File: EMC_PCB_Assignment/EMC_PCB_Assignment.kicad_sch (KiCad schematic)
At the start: 58 parts, among them IC1 LT8636JV#PBF, IC2 LP2985AIM5-3.0_NOPB, IC3 ATMEGA16U2-MU, IC4 ATMEGA328P-PU, IC5 OPA4350UA, J1 61300621121, J2 61300621121, J3 Header 8, J4 61300821121, J5 Header 10, J6 61300421121, J7 USB_B_Micro, Y1 16M, Y2 16M

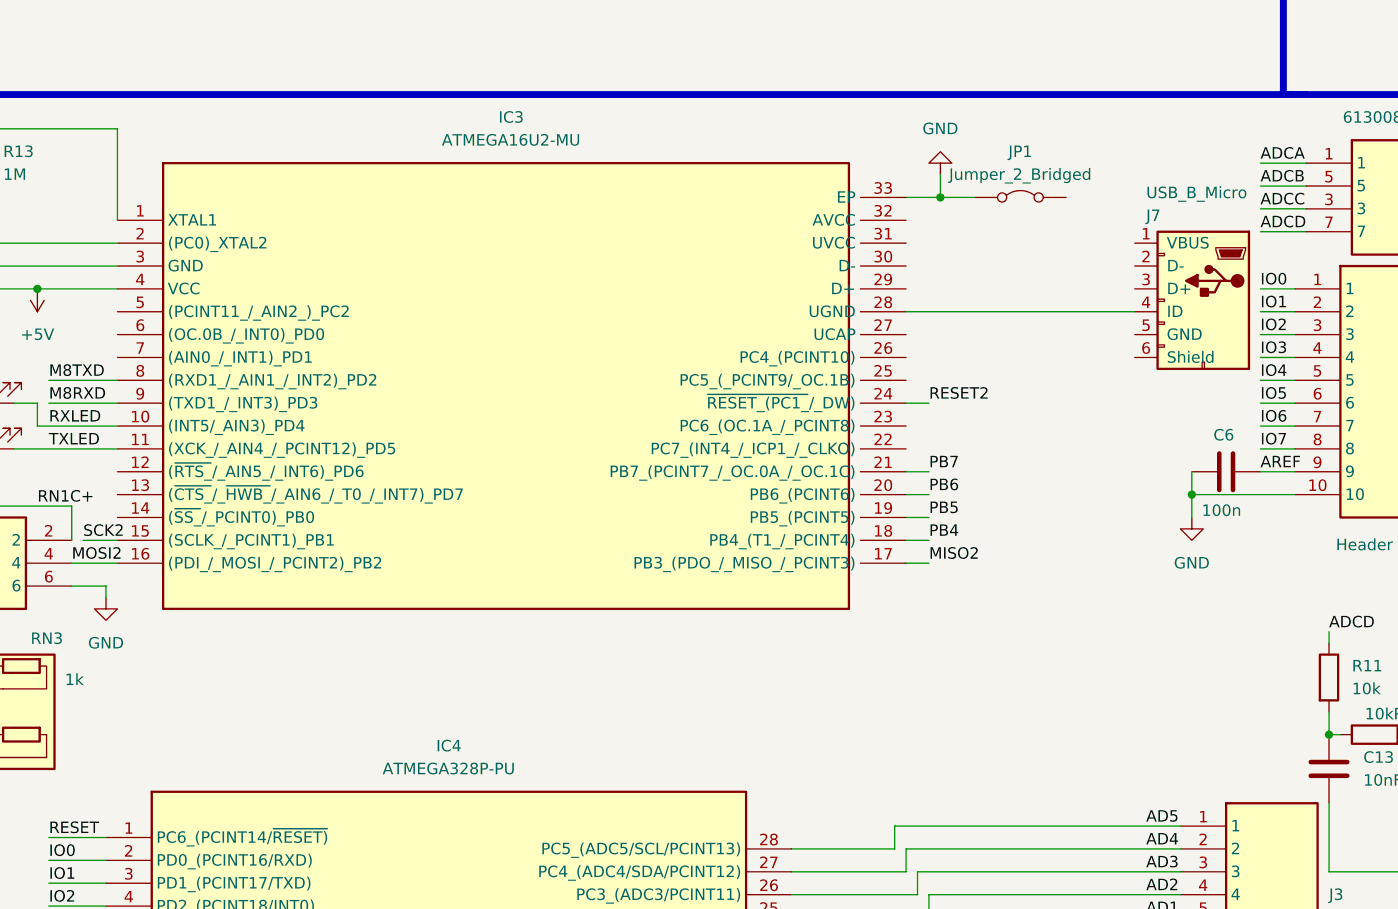
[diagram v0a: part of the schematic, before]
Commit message: Only LT8636 is still missing
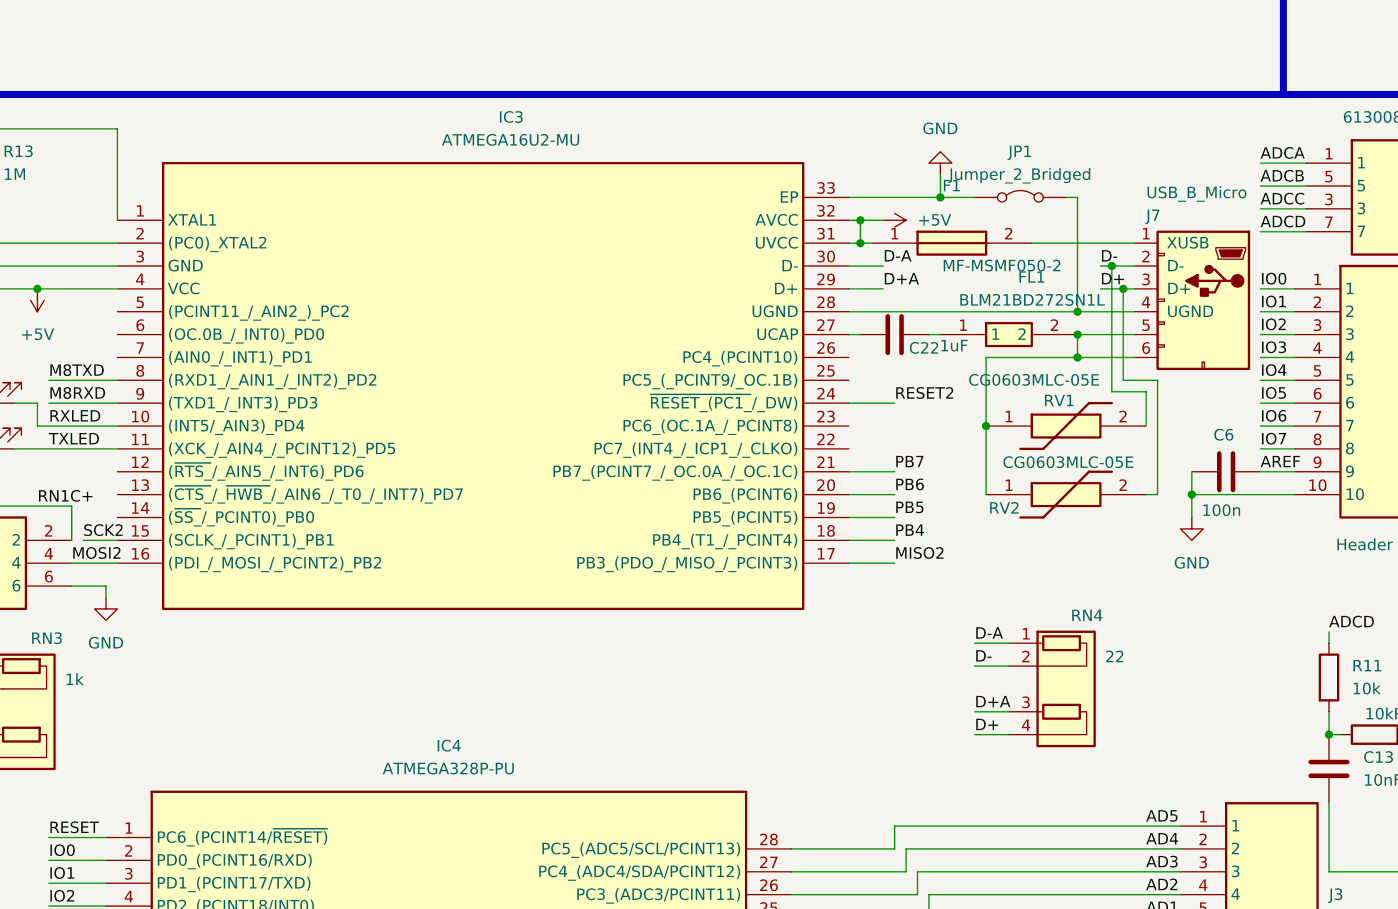
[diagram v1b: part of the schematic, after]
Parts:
- added C22: 1uF, symbol Device:C
- added F1: MF-MSMF050-2, FUSC4632X85N, symbol SamacSys_Parts:MF-MSMF050-2
- added FL1: BLM21BD272SN1L, BLM21BD222SH1K, symbol SamacSys_Parts:BLM21BD272SN1L
- added RN4: 22, Resistor_THT:R_Array_SIP4, symbol Device:R_Pack02_SIP
- added RV1, RV2: CG0603MLC-05E, VARC1608X55N, symbol SamacSys_Parts:CG0603MLC-05E
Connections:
- net +5V: now also IC3.31 (UVCC), IC3.32 (AVCC), F1.1
- net at IC3.27 (UCAP): now also C22.1
- net at IC3.28 (UGND), J7.4 (UGND): now also JP1.2 (B)
- net D+A: now reaches IC3.29 (D+)
- net D+A: now also RN4.3 (R2.1)
- net D-A: now reaches IC3.30 (D-)
- net D-A: now also RN4.1 (R1.1)
- net at J7.1 (XUSB): now also F1.2
- net D-: now reaches J7.2 (D-)
- net D-: now also RN4.2 (R1.2), RV1.2
- net D+: now reaches J7.3 (D+)
- net D+: now also RN4.4 (R2.2), RV2.2
- net at J7.5: now also J7.6, FL1.2, RV1.1, RV2.1
- new net: C22.2, FL1.1
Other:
- moved on the sheet: IC3

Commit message: Schematics Finished. I also put the imported Components in there. I was not sure if they are also in the project itself
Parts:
- removed RN1: 1k, Resistor_THT:R_Array_SIP4, symbol Device:R_Pack02_SIP
- added C, C29, C30: 1uF, symbol Device:C
- added C23, C24, C25: 10uF, symbol Device:C
- added C26: 100uF, symbol Device:C
- added C27: 0.1uF, symbol Device:C
- added C28: 10pF, symbol Device:C
- added D5: LED, symbol Device:LED
- added FB1: FerriteBead, symbol Device:FerriteBead
- added J8: Power Connector, SHDRRA2W80P0X350_1X2_1050X920X750P, symbol SamacSys_Parts:691305140002
- added L2: 0.33u, symbol Device:L
- added L3: 1.5u, symbol Device:L
- added R15: 1M, symbol Device:R
- added R16: 243k, symbol Device:R
- added R17: 17.8k, symbol Device:R
- added RN5: 1k, symbol Device:R_Pack04
- J1, J2: value 61300621121 -> 3x2 Connector
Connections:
- net +5V: now also IC1.2 (BIAS), C26.2, C28.2, L3.1, R15.2, RN5.7 (R2.2), RN5.8 (R1.2)
- net GND: now also IC1.4 (GND_1), C.1, C23.2, C24.2, C25.2, C26.1, D5.1 (K), J8.2
- net IO0: now also RN5.4 (R4.1)
- net IO1: now also RN5.3 (R3.1)
- net M8RXD: now also RN5.5 (R4.2)
- net M8TXD: now also RN5.6 (R3.2)
- net at IC1.10 (SW_3): now also IC1.8 (SW_1), IC1.9 (SW_2), C27.1, L3.2
- net VIN: now reaches IC1.11 (VIN_2)
- net VIN: now also IC1.14 (EN/UV), C30.1
- net at IC1.13 (GND_2): now also IC1.21 (GND_3), C29.2, C30.2, R16.2, R17.2
- net INTVCC: now reaches IC1.15 (SYNC/MODE)
- net INTVCC: now also IC1.3 (INTVCC), C29.1
- net at IC1.17 (RT): now also R17.1
- net FB: now reaches IC1.19 (FB_1)
- net FB: now also IC1.20 (FB_2), C28.1, R15.1, R16.1
- net at IC1.6 (VIN_1): now also C.2, C25.1, L2.2
- net at IC1.7 (BST): now also C27.2
- new net: C24.1, FB1.2, L2.1
- new net P_LED_IN: D5.2 (A), RN5.1 (R1.1), RN5.2 (R2.1)
- new net VCC: C23.1, FB1.1, J8.1
- no-connect marks 0 -> 17
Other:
- note added: "See RN5 on the Schematics"
- note added: "Vout (5V)"
- company: (none) -> Group 16
- title: (none) -> Microcontroller_PCB_Assignment
- moved on the sheet: IC1, RV1, RV2

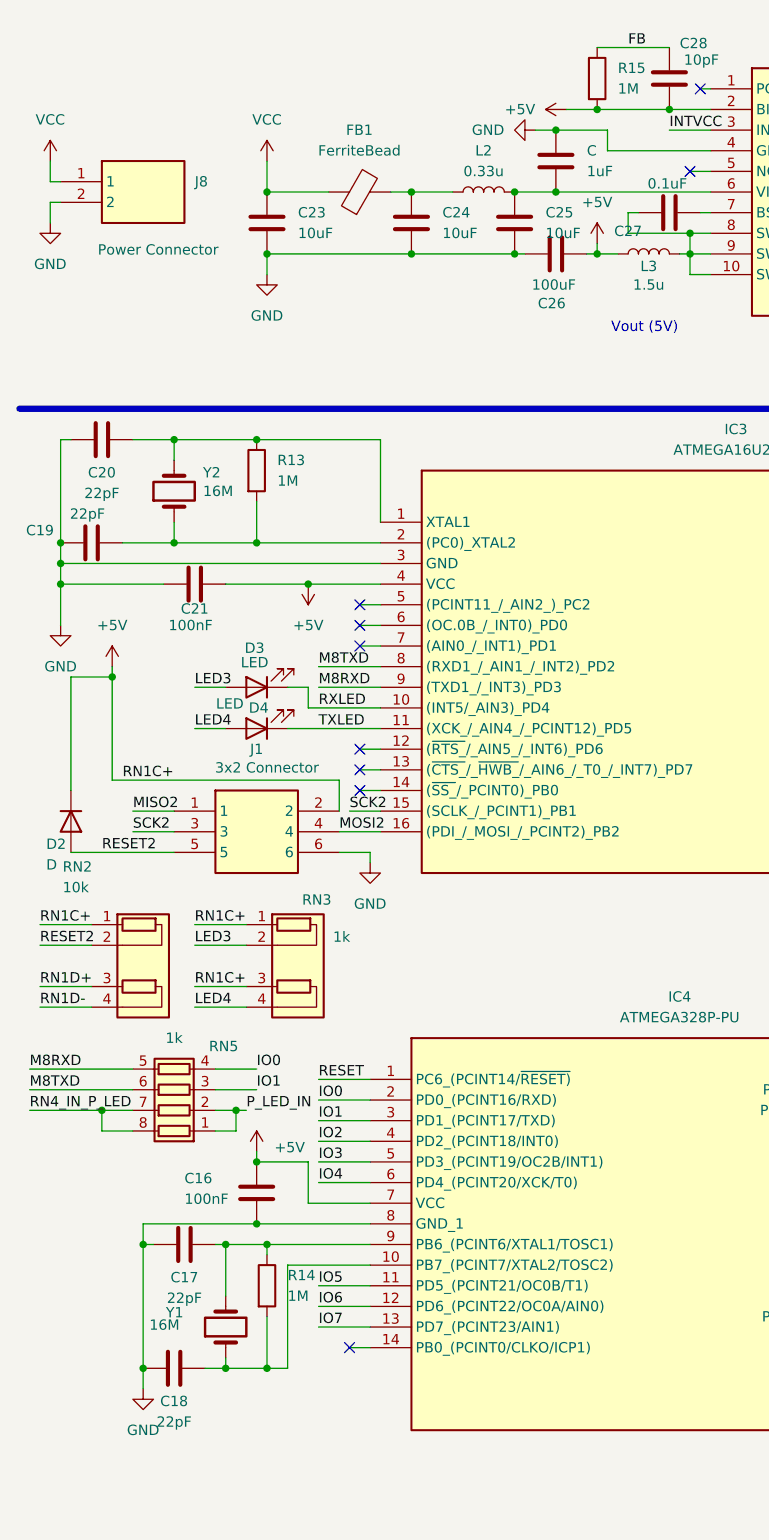
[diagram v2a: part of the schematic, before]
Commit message: Added Footprint libraries and footprints to all components
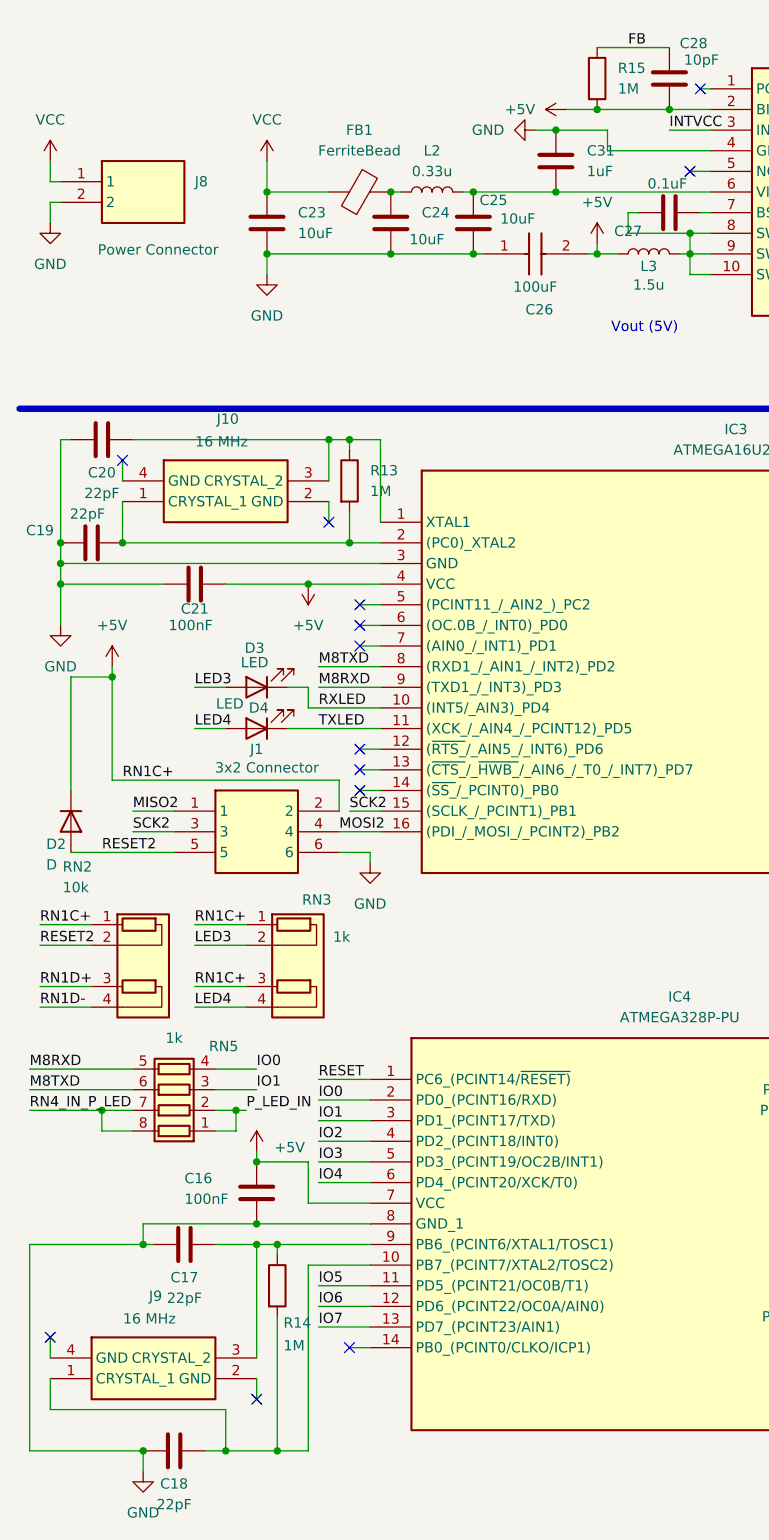
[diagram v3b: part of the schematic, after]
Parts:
- removed C26: 100uF, symbol Device:C
- removed Y1, Y2: 16M, symbol Device:Crystal
- added C26: 100uF, SamacSys_Parts:CAPPM3528X210N, symbol SamacSys_Parts:NOJB107M006RWJ
- added J10, J9: 16 MHz, SamacSys_Parts:LFXTAL062487Cutt, symbol SamacSys_Parts:LFXTAL062487Cutt
- C1, C10, C11, C12, C13, C14, C15, C16, C17, C18, C19, C2, C20, C21, C22, C23, C24, C25, C27, C28, C29, C3, C30, C4, C5, C6, C7, C8, C9: footprint (none) -> Capacitor_SMD:C_0402_1005Metric
- C31: renamed from C; footprint (none) -> Capacitor_SMD:C_0402_1005Metric
- D1, D2: footprint (none) -> Diode_SMD:D_0402_1005Metric
- D3, D4, D5: footprint (none) -> LED_SMD:LED_0402_1005Metric
- F1: footprint FUSC4632X85N -> SamacSys_Parts:FUSC4632X85N
- FB1: footprint (none) -> Ferrite_THT:LairdTech_28C0236-0JW-10
- FL1: footprint BLM21BD222SH1K -> SamacSys_Parts:BLM21BD222SH1K
- IC1: footprint LT8636JVPBF -> SamacSys_Parts:LT8636JVPBF
- IC2: footprint SOT95P280X145-5N -> SamacSys_Parts:SOT95P280X145-5N
- IC3: footprint QFN50P500X500X100-33N-D -> SamacSys_Parts:QFN50P500X500X100-33N-D
- IC4: footprint DIP794W53P254L3467H457Q28N -> SamacSys_Parts:DIP794W53P254L3467H457Q28N
- IC5: footprint SOIC127P600X175-14N -> SamacSys_Parts:SOIC127P600X175-14N
- J1, J2: footprint HDRV6W64P254_2X3_762X508X889P -> SamacSys_Parts:HDRV6W64P254_2X3_762X508X889P
- J3: footprint HDRV8W64P0X254_1X8_2032X254X854P -> SamacSys_Parts:HDRV8W64P0X254_1X8_2032X254X854P
- J4: footprint 61300821121 -> SamacSys_Parts:61300821121
- J5: footprint HDRV10W64P0X254_1X10_2540X254X854P -> SamacSys_Parts:HDRV10W64P0X254_1X10_2540X254X854P
- J6: footprint HDRV4W64P254X254_2X2_508X508X854P -> SamacSys_Parts:HDRV4W64P254X254_2X2_508X508X854P
- J7: footprint (none) -> Connector_USB:USB_Micro-B_Amphenol_10104110_Horizontal
- J8: footprint SHDRRA2W80P0X350_1X2_1050X920X750P -> SamacSys_Parts:SHDRRA2W80P0X350_1X2_1050X920X750P
- JP1: footprint (none) -> Jumper:SolderJumper-2_P1.3mm_Bridged_Pad1.0x1.5mm
- L1, L2, L3: footprint (none) -> Inductor_SMD:L_0805_2012Metric
- R1, R10, R11, R12, R13, R14, R15, R16, R17, R2, R3, R4, R5, R6, R7, R8, R9: footprint (none) -> Resistor_SMD:R_01005_0402Metric
- RN5: footprint (none) -> Resistor_SMD:R_Array_Convex_4x0402
- RV1, RV2: footprint VARC1608X55N -> SamacSys_Parts:VARC1608X55N
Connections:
- net +5V: now also C26.2 (-)
- net GND: now also C26.1 (+)
- net at C19.2, IC3.2 ((PC0)_XTAL2), R13.2: now also J10.1 (CRYSTAL_1)
- net at C20.2, IC3.1 (XTAL1), R13.1: now also J10.3 (CRYSTAL_2)
- net at C18.2, IC4.10 (PB7_(PCINT7/XTAL2/TOSC2)), R14.2: now also J9.1 (CRYSTAL_1)
- net at C17.2, IC4.9 (PB6_(PCINT6/XTAL1/TOSC1)), R14.1: now also J9.3 (CRYSTAL_2)
- no-connect marks 17 -> 21
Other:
- moved on the sheet: C18, C24, C25, L2, R13, R14
